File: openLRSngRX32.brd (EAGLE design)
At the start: 48.6 x 48.2 mm, 49 parts, among them IC1 STM32F10XCXT6, IC2 REG1117, U1 MPU-6000QFN-24

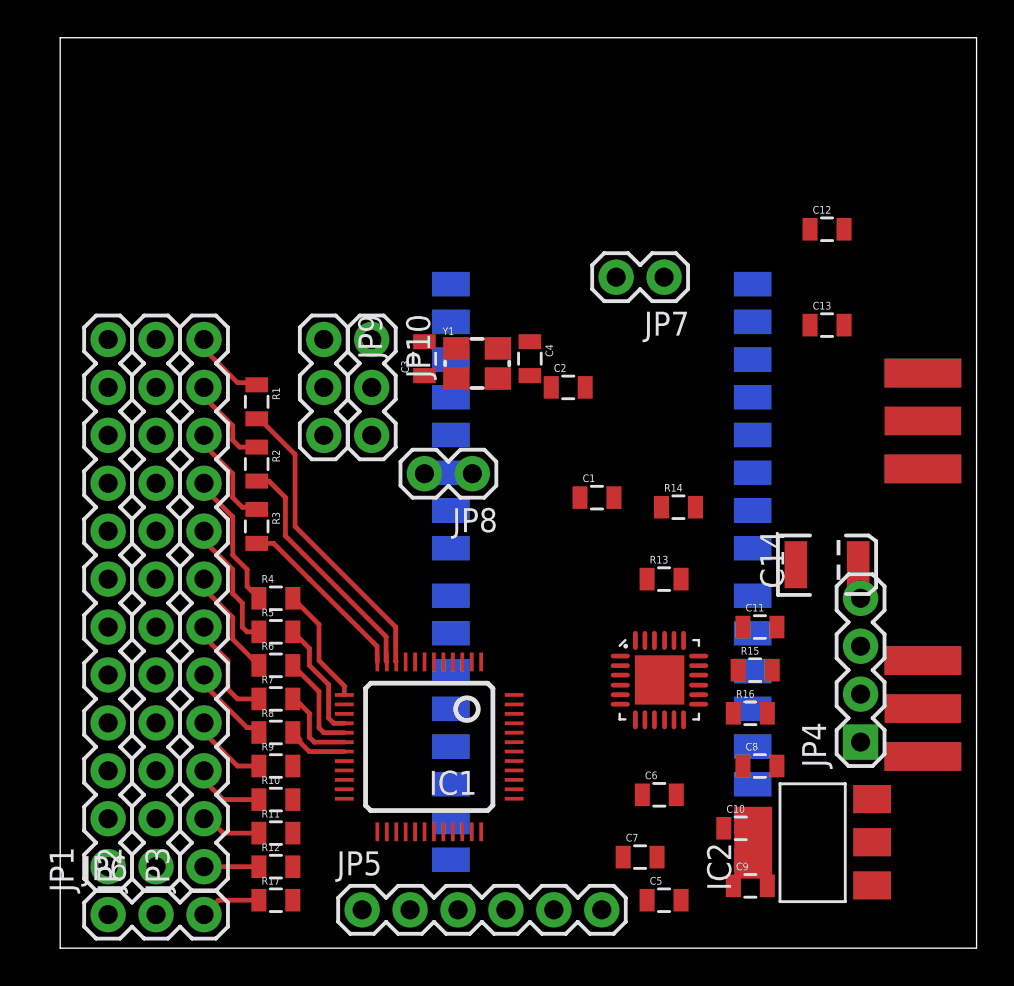
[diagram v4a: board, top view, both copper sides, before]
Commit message: Add .gitignore Board routing
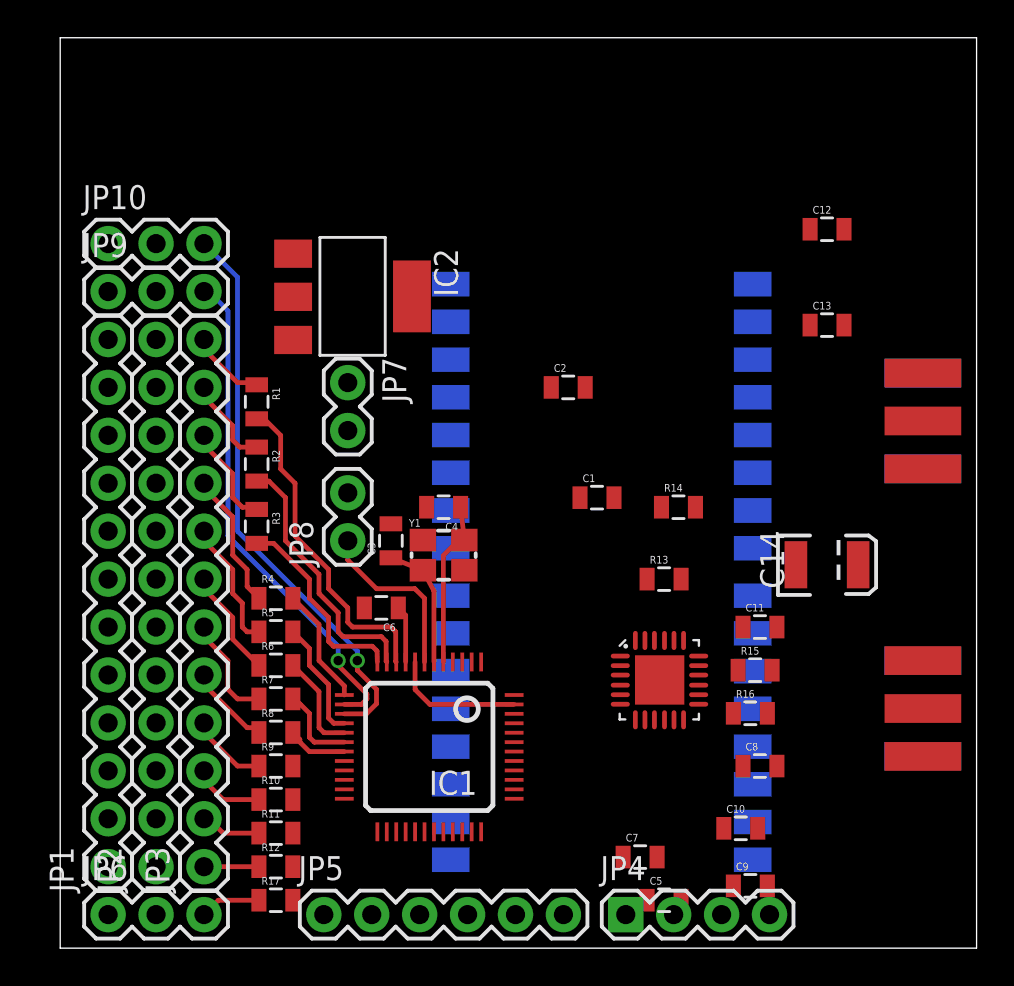
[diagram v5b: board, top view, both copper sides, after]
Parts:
- moved IC2 37.9 mm to (15.5, 34.5), turned to 270 degrees
- moved C6 17.8 mm to (17.0, 18.0), turned to 180 degrees
- moved JP7 17.7 mm to (15.2, 30.0), turned to 270 degrees
- moved JP4 15.4 mm to (30.0, 1.78), turned to 0 degrees
- moved JP10 14.9 mm to (2.54, 37.3), turned to 0 degrees
- moved JP9 11.7 mm to (2.54, 34.8), turned to 0 degrees
- moved Y1 10.3 mm to (20.3, 20.8)
- moved C3 9.81 mm to (17.5, 21.6)
- moved C4 9.11 mm to (20.3, 23.4), turned to 180 degrees
- moved JP8 7.50 mm to (15.2, 21.6), turned to 90 degrees
- moved JP5 2.05 mm to (14.0, 1.78)
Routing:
- net AIN5: track 0.00 -> 30.1 mm, vias 0 -> 1
- net AIN4: track 0.00 -> 26.6 mm, vias 0 -> 1
- net RESET: track 0.00 -> 9.30 mm
- net N$16: track 0.00 -> 8.98 mm
- net GND: track 0.00 -> 7.04 mm
- net N$17: track 0.00 -> 6.83 mm
- net 3V3: track 0.00 -> 3.03 mm
- net PWM1: track 16.0 -> 17.5 mm
- net PWM3: track 9.46 -> 10.7 mm
- net PWM2: track 12.8 -> 14.0 mm

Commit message: updates
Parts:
- added C15: (no value), SparkFun-Capacitors:0805
- moved C12 29.4 mm to (11.4, 34.5), turned to 90 degrees
- moved C13 27.7 mm to (13.0, 34.5), turned to 90 degrees
- moved R15 27.7 mm to (13.0, 28.7), turned to 270 degrees
- moved R16 25.0 mm to (17.5, 28.7), turned to 90 degrees
- moved C11 21.2 mm to (17.5, 25.1), turned to 90 degrees
- moved C14 20.7 mm to (25.7, 34.5), turned to 270 degrees
- moved R14 17.9 mm to (26.4, 6.60), turned to 270 degrees
- moved C7 15.8 mm to (15.0, 5.08), turned to 270 degrees
- moved C2 15.6 mm to (28.7, 14.2), turned to 180 degrees
- moved C10 14.6 mm to (24.6, 15.5)
- moved C1 13.7 mm to (34.3, 11.4), turned to 270 degrees
- moved R13 9.80 mm to (26.2, 11.7), turned to 90 degrees
- moved J$2 8.89 mm to (40.4, 32.5), flipped to the bottom
- moved C5 8.77 mm to (23.9, 5.84), turned to 270 degrees
- moved C9 8.07 mm to (39.9, 10.7), flipped to the bottom, turned to 180 degrees
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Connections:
- net 3V3: now also C15.1
- net GND: now also C15.2
- net PWM10: now also IC1.45; no longer IC1.43
- net PWM11: now also IC1.43; no longer IC1.45
- net PWM12: now also IC1.42; no longer IC1.46
- net PWM9: now also IC1.46; no longer IC1.42
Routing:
- net 3V3: track 3.03 -> 116.4 mm, vias 0 -> 4
- net VCC: track 0.00 -> 42.0 mm
- net MISO: track 0.00 -> 33.7 mm, vias 0 -> 3
- net MOSI: track 0.00 -> 32.8 mm, vias 0 -> 3
- net SCL: track 0.00 -> 31.6 mm, vias 0 -> 2
- net NSS: track 0.00 -> 30.4 mm, vias 0 -> 1
- net SCK: track 0.00 -> 28.8 mm, vias 0 -> 3
- net BOOT0: track 0.00 -> 27.2 mm
- net SDA: track 0.00 -> 24.6 mm, vias 0 -> 2
- net PWM12: track 0.00 -> 16.3 mm, vias 0 -> 2
- net PWM11: track 0.00 -> 15.4 mm, vias 0 -> 2
- net PWM10: track 0.00 -> 14.4 mm, vias 0 -> 2
- net PWM9: track 0.00 -> 14.2 mm, vias 0 -> 2
- net PPM: track 0.00 -> 12.8 mm
- net TX: track 0.00 -> 10.1 mm
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- added copper zone on layer 1, net GND
- added copper zone on layer 16, net GND
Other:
- board size 48.6 x 48.2 mm -> 43 x 39.6 mm

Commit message: board
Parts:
- moved R13 11.5 mm to (35.1, 4.32)
- moved R14 6.51 mm to (32.5, 4.32), turned to 90 degrees
- moved C10 1.48 mm to (23.9, 16.8), turned to 180 degrees
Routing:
- net 3V3: track 116.4 -> 156.4 mm, vias 4 -> 8
- net BOOT0: track 27.2 -> 29.0 mm
- net SCL: track 31.6 -> 32.5 mm
- net NSS: track 30.4 -> 29.6 mm
- net GND: vias 0 -> 2

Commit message: ...almost done
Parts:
- moved C10 0.80 mm to (24.1, 16.0), turned to 90 degrees
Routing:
- net N$20: track 0.00 -> 12.8 mm
- net N$19: track 0.00 -> 9.15 mm
- net 3V3: track 156.4 -> 162.4 mm
- net BOOT0: track 29.0 -> 25.7 mm, vias 0 -> 1
- net PWM9: track 14.2 -> 15.0 mm
- net GND: vias 2 -> 5
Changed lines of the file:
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@@
 <element name="C8" library="SparkFun-Capacitors" package="0805" value="" x="34.29" y="8.128" rot="R90"/>
 <element name="C9" library="SparkFun-Capacitors" package="0805" value="" x="39.878" y="10.668" rot="MR180"/>
-<element name="C10" library="SparkFun-Capacitors" package="0805" value="" x="23.876" y="16.764" rot="R180"/>
+<element name="C10" library="SparkFun-Capacitors" package="0805" value="" x="24.13" y="16.002" rot="R90"/>
 <element name="JP4" library="SparkFun-Connectors" package="1X04" value="" x="29.972" y="1.778"/>
 <element name="JP5" library="SparkFun-Connectors" package="1X06" value="" x="13.97" y="1.778"/>
@@
 <via x="28.194" y="7.366" extent="1-16" drill="0.5"/>
 <via x="33.02" y="7.112" extent="1-16" drill="0.5"/>
-<wire x1="21.42" y1="20.028" x2="20.702" y2="21.194" width="0" layer="19" extent="1-16"/>
-<wire x1="12.954" y1="29.602" x2="17.526" y2="26.046" width="0" layer="19" extent="1-1"/>
+<via x="10.922" y="31.75" extent="1-16" drill="0.5"/>
+<via x="13.208" y="25.908" extent="1-16" drill="0.5"/>
+<via x="26.924" y="15.24" extent="1-16" drill="0.5"/>
 </signal>
 <signal name="VCC">
@@
 <wire x1="22.606" y1="5.914" x2="22.562" y2="5.914" width="0.254" layer="1"/>
 <wire x1="22.562" y1="5.914" x2="22.308" y2="6.168" width="0.254" layer="1"/>
-<via x="28.194" y="15.748" extent="1-16" drill="0.5"/>
-<wire x1="28.194" y1="15.748" x2="28.194" y2="27.432" width="0.4064" layer="1"/>
+<via x="28.194" y="16.002" extent="1-16" drill="0.5"/>
+<wire x1="28.194" y1="16.002" x2="28.194" y2="27.432" width="0.4064" layer="1"/>
 <wire x1="28.194" y1="27.432" x2="24.003" y2="31.623" width="0.4064" layer="1"/>
 <wire x1="35.052" y1="5.218" x2="35.052" y2="6.35" width="0.4064" layer="1"/>
@@
 <via x="32.004" y="13.716" extent="1-16" drill="0.5"/>
 <wire x1="32.004" y1="13.716" x2="32.004" y2="6.35" width="0.4064" layer="16"/>
-<wire x1="28.194" y1="15.748" x2="29.972" y2="15.748" width="0.4064" layer="16"/>
-<wire x1="29.972" y1="15.748" x2="32.004" y2="13.716" width="0.4064" layer="16"/>
-<wire x1="24.014" y1="13.462" x2="24.776" y2="16.764" width="0" layer="19" extent="1-1"/>
-<wire x1="28.194" y1="15.748" x2="24.776" y2="16.764" width="0" layer="19" extent="1-1"/>
+<wire x1="28.194" y1="16.002" x2="29.718" y2="16.002" width="0.4064" layer="16"/>
+<wire x1="29.718" y1="16.002" x2="32.004" y2="13.716" width="0.4064" layer="16"/>
+<wire x1="24.014" y1="13.462" x2="24.014" y2="14.986" width="0.254" layer="1"/>
+<wire x1="24.014" y1="14.986" x2="24.13" y2="15.102" width="0.254" layer="1"/>
+<wire x1="28.194" y1="16.002" x2="26.416" y2="16.002" width="0.4064" layer="1"/>
+<wire x1="26.416" y1="16.002" x2="25.654" y2="15.24" width="0.4064" layer="1"/>
+<wire x1="25.654" y1="15.24" x2="24.268" y2="15.24" width="0.4064" layer="1"/>
+<wire x1="24.268" y1="15.24" x2="24.13" y2="15.102" width="0.4064" layer="1"/>
 </signal>
 <signal name="N$1">
@@
 <contactref element="R9" pad="2"/>
 <contactref element="IC1" pad="46"/>
-<wire x1="24.058" y1="12.418" x2="17.752" y2="12.418" width="0.254" layer="1"/>
-<wire x1="17.752" y1="12.418" x2="17.526" y2="12.7" width="0.254" layer="1"/>
-<via x="17.526" y="12.7" extent="1-16" drill="0.5"/>
-<wire x1="17.526" y1="12.7" x2="14.478" y2="12.7" width="0.254" layer="16"/>
-<wire x1="14.478" y1="12.7" x2="13.208" y2="11.43" width="0.254" layer="16"/>
+<wire x1="24.058" y1="12.418" x2="22.098" y2="12.446" width="0.254" layer="1"/>
+<wire x1="22.098" y1="12.446" x2="21.618" y2="12.926" width="0.254" layer="1"/>
+<via x="17.526" y="13.462" extent="1-16" drill="0.5"/>
+<wire x1="17.526" y1="13.462" x2="14.732" y2="13.462" width="0.254" layer="16"/>
+<wire x1="14.732" y1="13.462" x2="14.478" y2="13.208" width="0.254" layer="16"/>
+<wire x1="14.478" y1="13.208" x2="13.208" y2="11.43" width="0.254" layer="16"/>
 <wire x1="13.208" y1="11.43" x2="13.208" y2="9.652" width="0.254" layer="16"/>
 <via x="13.208" y="9.652" extent="1-16" drill="0.5"/>
 <wire x1="13.208" y1="9.652" x2="12.33" y2="9.652" width="0.254" layer="1"/>
+<wire x1="21.618" y1="12.926" x2="18.006" y2="12.926" width="0.254" layer="1"/>
+<wire x1="18.006" y1="12.926" x2="17.526" y2="13.462" width="0.254" layer="1"/>
 </signal>
 <signal name="PWM10">
 <contactref element="R10" pad="2"/>
 <contactref element="IC1" pad="45"/>
-<wire x1="24.058" y1="11.918" x2="18.014" y2="11.918" width="0.254" layer="1"/>
-<wire x1="18.014" y1="11.918" x2="17.78" y2="11.684" width="0.254" layer="1"/>
-<via x="17.78" y="11.684" extent="1-16" drill="0.5"/>
-<wire x1="17.78" y1="11.684" x2="14.732" y2="11.684" width="0.254" layer="16"/>
-<wire x1="14.732" y1="11.684" x2="13.97" y2="10.922" width="0.254" layer="16"/>
+<wire x1="24.058" y1="11.918" x2="21.844" y2="11.938" width="0.254" layer="1"/>
+<wire x1="21.844" y1="11.938" x2="21.356" y2="12.426" width="0.254" layer="1"/>
+<wire x1="21.356" y1="12.426" x2="20.808" y2="12.426" width="0.254" layer="1"/>
+<wire x1="20.808" y1="12.426" x2="17.272" y2="12.446" width="0.254" layer="1"/>
+<via x="17.272" y="12.446" extent="1-16" drill="0.5"/>
+<wire x1="17.272" y1="12.446" x2="15.494" y2="12.446" width="0.254" layer="16"/>
+<wire x1="15.494" y1="12.446" x2="13.97" y2="10.922" width="0.254" layer="16"/>
 <wire x1="13.97" y1="10.922" x2="13.97" y2="9.144" width="0.254" layer="16"/>
 <wire x1="13.97" y1="9.144" x2="13.208" y2="8.382" width="0.254" layer="16"/>
@@
 <wire x1="16.764" y1="8.89" x2="17.78" y2="9.906" width="0.254" layer="16"/>
 <wire x1="17.78" y1="9.906" x2="18.034" y2="9.906" width="0.254" layer="16"/>
-<wire x1="18.034" y1="9.906" x2="18.542" y2="10.414" width="0.254" layer="16"/>
-<wire x1="18.542" y1="10.414" x2="18.542" y2="11.43" width="0.254" layer="16"/>
-<wire x1="18.542" y1="11.43" x2="19.304" y2="12.192" width="0.254" layer="16"/>
-<wire x1="19.304" y1="12.192" x2="19.812" y2="12.192" width="0.254" layer="16"/>
+<wire x1="18.034" y1="9.906" x2="19.304" y2="11.176" width="0.254" layer="16"/>
+<wire x1="19.304" y1="11.176" x2="19.304" y2="11.938" width="0.254" layer="16"/>
+<wire x1="19.304" y1="11.938" x2="19.812" y2="12.192" width="0.254" layer="16"/>
 <wire x1="19.812" y1="12.192" x2="20.304" y2="12.684" width="0.254" layer="16"/>
 <wire x1="20.304" y1="12.684" x2="20.702" y2="12.684" width="0.254" layer="16"/>
@@
 <wire x1="12.954" y1="27.802" x2="14.87" y2="27.802" width="0.254" layer="1"/>
 <wire x1="14.87" y1="27.802" x2="15.24" y2="27.432" width="0.254" layer="1" curve="-90"/>
-<wire x1="24.058" y1="11.418" x2="26.404" y2="11.418" width="0.254" layer="1"/>
-<wire x1="26.404" y1="11.418" x2="26.67" y2="11.684" width="0.254" layer="1"/>
-<wire x1="26.67" y1="11.684" x2="26.67" y2="16.256" width="0.254" layer="1"/>
-<wire x1="26.67" y1="16.256" x2="24.638" y2="20.828" width="0.254" layer="1"/>
-<wire x1="24.638" y1="20.828" x2="22.352" y2="23.114" width="0.254" layer="1"/>
-<wire x1="22.352" y1="23.114" x2="22.352" y2="24.892" width="0.254" layer="1"/>
-<wire x1="22.352" y1="24.892" x2="18.542" y2="28.702" width="0.254" layer="1"/>
-<wire x1="18.542" y1="28.702" x2="16.51" y2="28.702" width="0.254" layer="1"/>
-<wire x1="16.51" y1="28.702" x2="15.24" y2="27.432" width="0.254" layer="1"/>
+<wire x1="24.058" y1="11.418" x2="18.3" y2="11.418" width="0.254" layer="1"/>
+<wire x1="18.3" y1="11.418" x2="18.034" y2="11.684" width="0.254" layer="1"/>
+<via x="18.034" y="11.684" extent="1-16" drill="0.5"/>
+<wire x1="18.034" y1="11.684" x2="18.034" y2="12.446" width="0.254" layer="16"/>
+<wire x1="18.034" y1="12.446" x2="18.288" y2="12.7" width="0.254" layer="16"/>
+<wire x1="18.288" y1="12.7" x2="18.288" y2="14.478" width="0.254" layer="16"/>
+<wire x1="18.288" y1="14.478" x2="17.272" y2="15.494" width="0.254" layer="16"/>
+<wire x1="17.272" y1="15.494" x2="17.272" y2="25.4" width="0.254" layer="16"/>
+<wire x1="17.272" y1="25.4" x2="15.24" y2="27.432" width="0.254" layer="16"/>
 </signal>
 <signal name="DTR">
@@
 <contactref element="U$2" pad="4"/>
 <contactref element="U$2" pad="6"/>
-<wire x1="36.702" y1="25.194" x2="36.702" y2="29.194" width="0" layer="19" extent="16-16"/>
+<wire x1="36.702" y1="25.194" x2="34.242" y2="25.194" width="0.254" layer="16"/>
+<wire x1="34.242" y1="25.194" x2="33.782" y2="25.654" width="0.254" layer="16"/>
+<wire x1="33.782" y1="25.654" x2="33.782" y2="28.448" width="0.254" layer="16"/>
+<wire x1="33.782" y1="28.448" x2="34.544" y2="29.21" width="0.254" layer="16"/>
+<wire x1="34.544" y1="29.21" x2="36.686" y2="29.21" width="0.254" layer="16"/>
+<wire x1="36.686" y1="29.21" x2="36.702" y2="29.194" width="0.254" layer="16"/>
 </signal>
 <signal name="N$20">
 <contactref element="U$2" pad="7"/>
 <contactref element="U$2" pad="3"/>
-<wire x1="36.702" y1="23.194" x2="36.702" y2="31.194" width="0" layer="19" extent="16-16"/>
+<wire x1="36.702" y1="23.194" x2="35.226" y2="23.194" width="0.254" layer="16"/>
+<wire x1="35.226" y1="23.194" x2="33.02" y2="25.4" width="0.254" layer="16"/>
+<wire x1="33.02" y1="25.4" x2="33.02" y2="28.956" width="0.254" layer="16"/>
+<wire x1="33.02" y1="28.956" x2="35.306" y2="31.242" width="0.254" layer="16"/>
+<wire x1="35.306" y1="31.242" x2="36.654" y2="31.242" width="0.254" layer="16"/>
+<wire x1="36.654" y1="31.242" x2="36.702" y2="31.194" width="0.254" layer="16"/>
 </signal>
 <signal name="N$23">
